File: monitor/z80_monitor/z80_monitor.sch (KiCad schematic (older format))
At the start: 0 parts

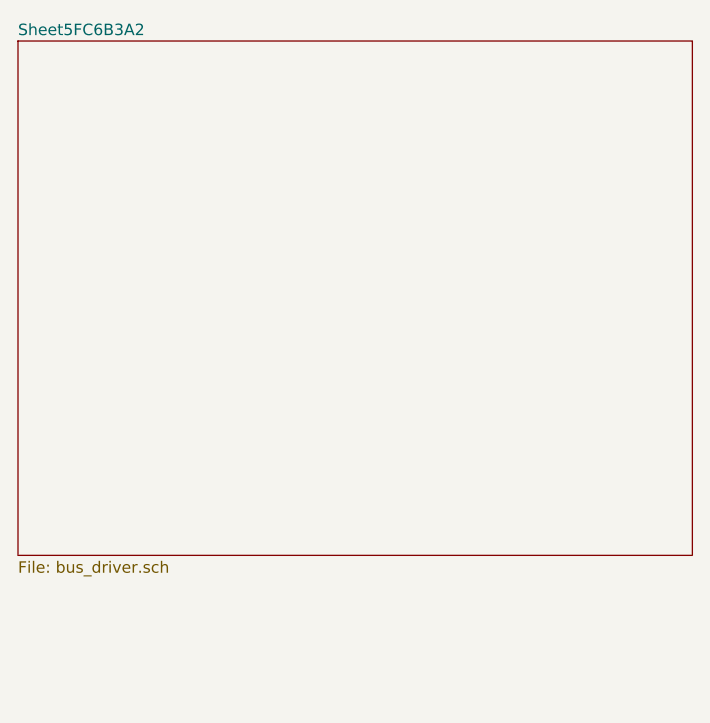
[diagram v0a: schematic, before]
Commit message: Assign some footprints and begin to play with layout
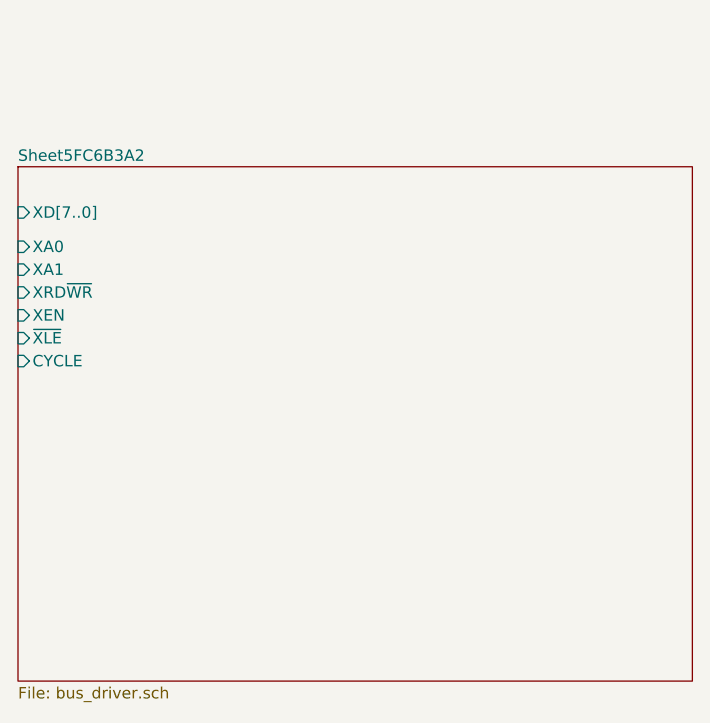
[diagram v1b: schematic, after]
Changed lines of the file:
@@
 $EndDescr
 $Sheet
-S 3150 2400 2950 2250
+S 3150 2950 2950 2250
 U 5FC6B3A3
 F0 "Sheet5FC6B3A2" 50
 F1 "bus_driver.sch" 50
+F2 "XD[7..0]" I L 3150 3150 50
+F3 "XA0" I L 3150 3300 50
+F4 "XA1" I L 3150 3400 50
+F5 "XRD~WR~" I L 3150 3500 50
+F6 "XEN" I L 3150 3600 50
+F7 "~XLE~" I L 3150 3700 50
+F8 "CYCLE" I L 3150 3800 50
 $EndSheet
 $EndSCHEMATC

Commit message: More updates.
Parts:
- added U13: ATmega328P-PU, Housings_DIP:DIP-28_W7.62mm, symbol MCU_Microchip_ATmega:ATmega328P-PU
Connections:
- new net: U13.22 (GND), U13.8 (GND)
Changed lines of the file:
@@
 $EndDescr
 $Sheet
-S 3150 2950 2950 2250
+S 5650 2950 2950 2250
 U 5FC6B3A3
 F0 "Sheet5FC6B3A2" 50
 F1 "bus_driver.sch" 50
-F2 "XD[7..0]" I L 3150 3150 50
-F3 "XA0" I L 3150 3300 50
-F4 "XA1" I L 3150 3400 50
-F5 "XRD~WR~" I L 3150 3500 50
-F6 "XEN" I L 3150 3600 50
-F7 "~XLE~" I L 3150 3700 50
-F8 "CYCLE" I L 3150 3800 50
+F2 "XD[7..0]" I L 5650 3150 50
+F3 "XA0" I L 5650 3300 50
+F4 "XA1" I L 5650 3400 50
+F5 "XRD~WR~" I L 5650 3500 50
+F6 "XEN" I L 5650 3600 50
+F7 "~XLE~" I L 5650 3700 50
+F8 "CYCLE" I L 5650 3800 50
 $EndSheet
+$Comp
+L MCU_Microchip_ATmega:ATmega328P-PU U13
+U 1 1 5FCDC4A1
+P 3200 4200
+F 0 "U13" H 2556 4246 50  0000 R CNN
+F 1 "ATmega328P-PU" H 2556 4155 50  0000 R CNN
+F 2 "Housings_DIP:DIP-28_W7.62mm" H 3200 4200 50  0001 C CIN
+F 3 "http://ww1.microchip.com/downloads/en/DeviceDoc/ATmega328_P%20AVR%20MCU%20with%20picoPower%20Technology%20Data%20Sheet%2040001984A.pdf" H 3200 4200 50  0001 C CNN
+	1    3200 4200
+	1    0    0    -1
+$EndComp
 $EndSCHEMATC
